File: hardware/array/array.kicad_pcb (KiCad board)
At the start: 2 copper layers, 70 x 100 mm, 165 parts, among them J1 Conn_01x04, J2 Conn_01x05, J3 Conn_01x05, P1 USB_C_Plug_USB2.0, U1 AMS1117-3.3, U2 STM32F103CBTx, Y1 8MHz

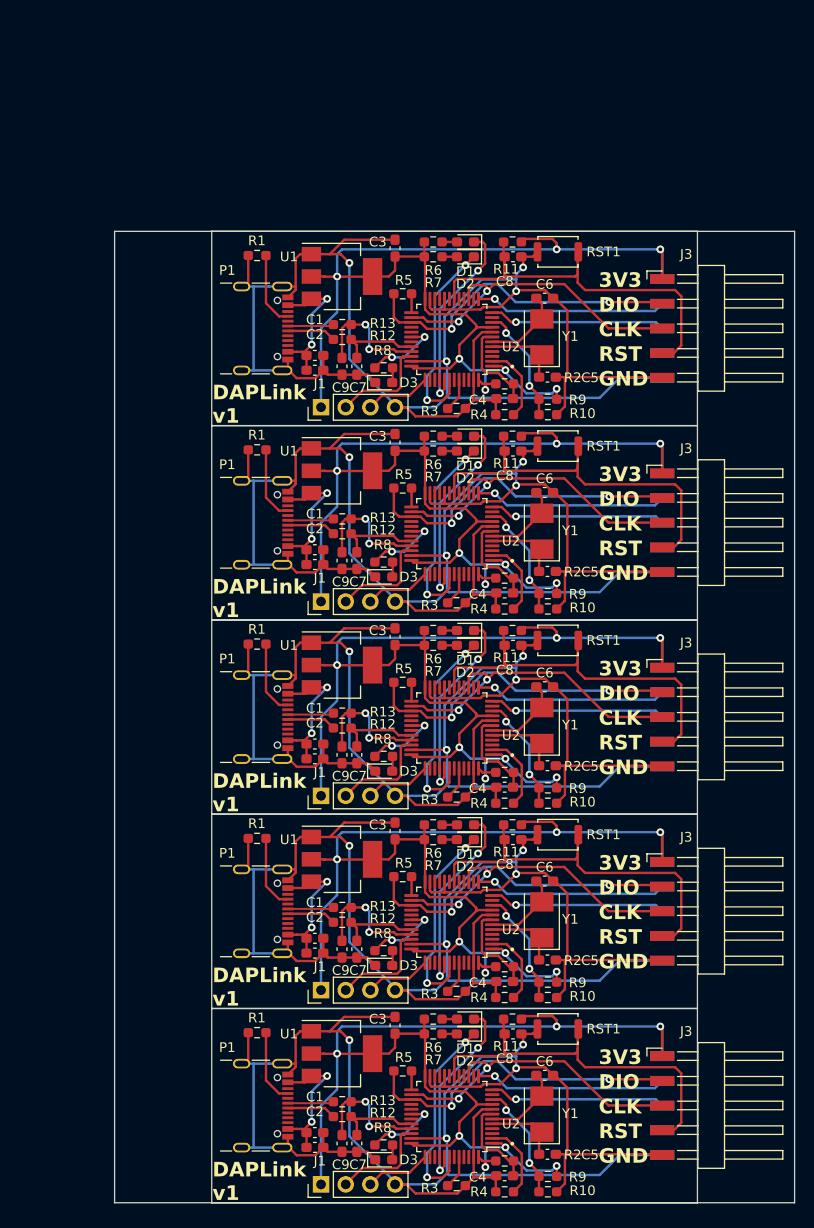
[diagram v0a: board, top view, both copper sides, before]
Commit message: feat(hw/usb): create board array
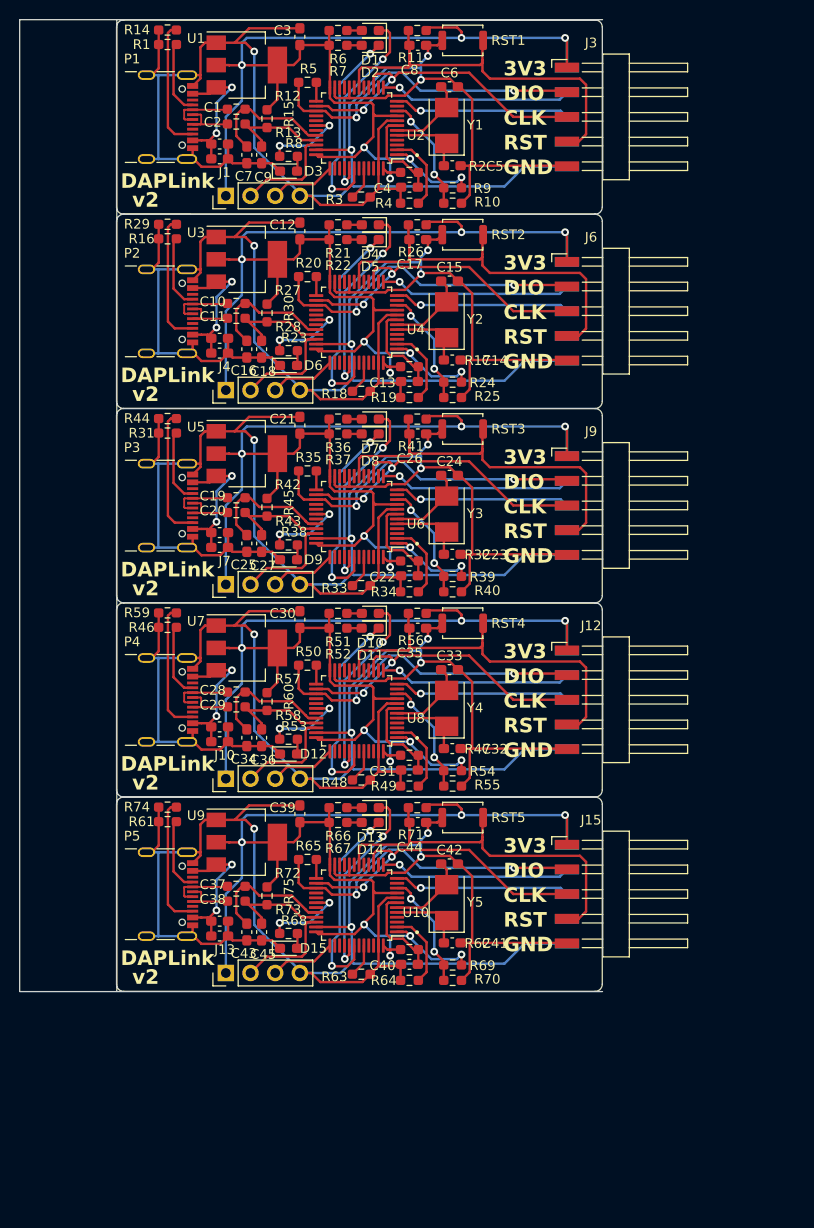
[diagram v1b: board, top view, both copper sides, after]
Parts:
- removed the C1 at (70.6, 82.8)
- removed the C1 at (70.6, 102.8)
- removed the C1 at (70.6, 142.8)
- removed the C1 at (70.6, 162.8)
- removed the C1 at (70.6, 122.8)
- removed the C2 at (70.6, 104.3)
- removed the C2 at (70.6, 144.3)
- removed the C2 at (70.6, 124.3)
- removed the C2 at (70.6, 164.3)
- removed the C2 at (70.6, 84.3)
- removed the C3 at (78.9, 71.7)
- removed the C3 at (78.9, 111.7)
- removed the C3 at (78.9, 131.7)
- removed the C3 at (78.9, 151.7)
- removed the C3 at (78.9, 91.7)
- removed the C4 at (90.2, 167.2)
- removed the C4 at (90.2, 127.2)
- removed the C4 at (90.2, 147.2)
- removed the C4 at (90.2, 107.2)
- removed the C4 at (90.2, 87.2)
- removed the C5 at (94.6, 85.0)
- removed the C5 at (94.6, 105.0)
- removed the C5 at (94.6, 125.0)
- removed the C5 at (94.6, 145.0)
- removed the C5 at (94.6, 165.0)
- removed the C6 at (94.3, 156.9)
- removed the C6 at (94.3, 76.9)
- removed the C6 at (94.3, 136.9)
- removed the C6 at (94.3, 96.9)
- removed the C6 at (94.3, 116.9)
- removed the C7 at (74.9, 83.9)
- removed the C7 at (74.9, 123.9)
- removed the C7 at (74.9, 163.9)
- removed the C7 at (74.9, 143.9)
- removed the C7 at (74.9, 103.9)
- removed the C8 at (91.0, 92.6)
- removed the C8 at (91.0, 132.6)
- removed the C8 at (91.0, 72.6)
- removed the C8 at (91.0, 112.6)
- removed the C8 at (91.0, 152.6)
- removed the C9 at (73.4, 143.9)
- removed the C9 at (73.4, 103.9)
- removed the C9 at (73.4, 123.9)
- removed the C9 at (73.4, 83.9)
- removed the C9 at (73.4, 163.9)
- removed the D1 at (86.1, 151.1)
- removed the D1 at (86.1, 131.1)
- removed the D1 at (86.1, 111.1)
- removed the D1 at (86.1, 71.1)
- removed the D1 at (86.1, 91.1)
- removed the D2 at (86.1, 92.6)
- removed the D2 at (86.1, 112.6)
- removed the D2 at (86.1, 152.6)
- removed the D2 at (86.1, 132.6)
- removed the D2 at (86.1, 72.6)
- removed the D3 at (77.7, 85.6)
- removed the D3 at (77.7, 125.6)
- removed the D3 at (77.7, 165.6)
- removed the D3 at (77.7, 145.6)
- removed the D3 at (77.7, 105.6)
- removed the J1 at (71.3, 88.1)
- removed the J1 at (71.3, 148.1)
- removed the J1 at (71.3, 168.1)
- removed the J1 at (71.3, 108.1)
- removed the J1 at (71.3, 128.1)
- removed the J2 at (111.9, 100.0)
- removed the J2 at (111.9, 140.0)
- removed the J2 at (111.9, 80.0)
- removed the J2 at (111.9, 160.0)
- removed the J2 at (111.9, 120.0)
- removed the J3 at (111.9, 100.0)
- removed the J3 at (111.9, 80.0)
- removed the J3 at (111.9, 140.0)
- removed the J3 at (111.9, 160.0)
- removed the J3 at (111.9, 120.0)
- removed the P1 at (64.2, 120.0)
- removed the P1 at (64.2, 80.0)
- removed the P1 at (64.2, 140.0)
- removed the P1 at (64.2, 160.0)
- removed the P1 at (64.2, 100.0)
- removed the R1 at (64.7, 152.5)
- removed the R1 at (64.7, 112.5)
- removed the R1 at (64.7, 92.5)
- removed the R1 at (64.7, 72.5)
- removed the R1 at (64.7, 132.5)
- removed the R10 at (94.6, 168.9)
- removed the R10 at (94.6, 108.9)
- removed the R10 at (94.6, 88.9)
- removed the R10 at (94.6, 128.9)
- removed the R10 at (94.6, 148.9)
- removed the R11 at (91.0, 151.1)
- removed the R11 at (91.0, 111.1)
- removed the R11 at (91.0, 71.1)
- removed the R11 at (91.0, 91.1)
- removed the R11 at (91.0, 131.1)
- removed the R12 at (73.4, 81.1)
- removed the R12 at (73.4, 121.1)
- removed the R12 at (73.4, 101.1)
- removed the R12 at (73.4, 141.1)
- removed the R12 at (73.4, 161.1)
- removed the R13 at (73.4, 79.6)
- removed the R13 at (73.4, 99.6)
- removed the R13 at (73.4, 159.6)
- removed the R13 at (73.4, 139.6)
- removed the R13 at (73.4, 119.6)
- removed the R2 at (90.2, 105.7)
- removed the R2 at (90.2, 145.7)
- removed the R2 at (90.2, 125.7)
- removed the R2 at (90.2, 85.7)
- removed the R2 at (90.2, 165.7)
- removed the R3 at (85.2, 108.2)
- removed the R3 at (85.2, 88.2)
- removed the R3 at (85.2, 148.2)
- removed the R3 at (85.2, 168.2)
- removed the R3 at (85.2, 128.2)
- removed the R4 at (90.2, 88.9)
- removed the R4 at (90.2, 148.9)
- removed the R4 at (90.2, 108.9)
- removed the R4 at (90.2, 168.9)
- removed the R4 at (90.2, 128.9)
- removed the R5 at (79.7, 136.4)
- removed the R5 at (79.7, 116.4)
- removed the R5 at (79.7, 96.4)
- removed the R5 at (79.7, 156.4)
- removed the R5 at (79.7, 76.4)
- removed the R6 at (82.8, 111.1)
- removed the R6 at (82.8, 151.1)
- removed the R6 at (82.8, 91.1)
- removed the R6 at (82.8, 71.1)
- removed the R6 at (82.8, 131.1)
- removed the R7 at (82.8, 152.6)
- removed the R7 at (82.8, 132.6)
- removed the R7 at (82.8, 92.6)
- removed the R7 at (82.8, 112.6)
- removed the R7 at (82.8, 72.6)
- removed the R8 at (77.7, 104.0)
- removed the R8 at (77.7, 84.0)
- removed the R8 at (77.7, 144.0)
- removed the R8 at (77.7, 164.0)
- removed the R8 at (77.7, 124.0)
- removed the R9 at (94.6, 87.3)
- removed the R9 at (94.6, 127.3)
- removed the R9 at (94.6, 107.3)
- removed the R9 at (94.6, 167.3)
- removed the R9 at (94.6, 147.3)
- removed the RST1 at (95.6, 72.1)
- removed the RST1 at (95.6, 92.1)
- removed the RST1 at (95.6, 132.1)
- removed the RST1 at (95.6, 152.1)
- removed the RST1 at (95.6, 112.1)
- removed the U1 at (73.4, 114.6)
- removed the U1 at (73.4, 94.6)
- removed the U1 at (73.4, 154.6)
- removed the U1 at (73.4, 74.6)
- removed the U1 at (73.4, 134.6)
- removed the U2 at (84.7, 161.1)
- removed the U2 at (84.7, 141.1)
- removed the U2 at (84.7, 101.1)
- removed the U2 at (84.7, 81.1)
- removed the U2 at (84.7, 121.1)
- removed the Y1 at (94.0, 100.9)
- removed the Y1 at (94.0, 80.9)
- removed the Y1 at (94.0, 160.9)
- removed the Y1 at (94.0, 140.9)
- removed the Y1 at (94.0, 120.9)
- added C1: 10nF, Capacitor_SMD:C_0603_1608Metric_Pad1.08x0.95mm_HandSolder, F.Cu at (60.8, 61.0)
- added C10: 10nF, Capacitor_SMD:C_0603_1608Metric_Pad1.08x0.95mm_HandSolder, F.Cu at (60.8, 81.0)
- added C11: 10uF, Capacitor_SMD:C_0603_1608Metric_Pad1.08x0.95mm_HandSolder, F.Cu at (60.8, 82.5)
- added C12: 10uF, Capacitor_SMD:C_0603_1608Metric_Pad1.08x0.95mm_HandSolder, F.Cu at (69.1, 70.0)
- added C13: 10nF, Capacitor_SMD:C_0603_1608Metric_Pad1.08x0.95mm_HandSolder, F.Cu at (80.4, 85.5)
- added C14: 20pF, Capacitor_SMD:C_0603_1608Metric_Pad1.08x0.95mm_HandSolder, F.Cu at (84.8, 83.2)
- added C15: 20pF, Capacitor_SMD:C_0603_1608Metric_Pad1.08x0.95mm_HandSolder, F.Cu at (84.5, 75.1)
- added C16: 18pF, Capacitor_SMD:C_0603_1608Metric_Pad1.08x0.95mm_HandSolder, F.Cu at (63.6, 82.1)
- added C17: 10nF, Capacitor_SMD:C_0603_1608Metric_Pad1.08x0.95mm_HandSolder, F.Cu at (81.2, 70.9)
- added C18: 18pF, Capacitor_SMD:C_0603_1608Metric_Pad1.08x0.95mm_HandSolder, F.Cu at (65.1, 82.1)
- added C19: 10nF, Capacitor_SMD:C_0603_1608Metric_Pad1.08x0.95mm_HandSolder, F.Cu at (60.8, 101.0)
- added C2: 10uF, Capacitor_SMD:C_0603_1608Metric_Pad1.08x0.95mm_HandSolder, F.Cu at (60.8, 62.5)
- added C20: 10uF, Capacitor_SMD:C_0603_1608Metric_Pad1.08x0.95mm_HandSolder, F.Cu at (60.8, 102.5)
- added C21: 10uF, Capacitor_SMD:C_0603_1608Metric_Pad1.08x0.95mm_HandSolder, F.Cu at (69.1, 90.0)
- added C22: 10nF, Capacitor_SMD:C_0603_1608Metric_Pad1.08x0.95mm_HandSolder, F.Cu at (80.4, 105.5)
- added C23: 20pF, Capacitor_SMD:C_0603_1608Metric_Pad1.08x0.95mm_HandSolder, F.Cu at (84.8, 103.2)
- added C24: 20pF, Capacitor_SMD:C_0603_1608Metric_Pad1.08x0.95mm_HandSolder, F.Cu at (84.5, 95.1)
- added C25: 18pF, Capacitor_SMD:C_0603_1608Metric_Pad1.08x0.95mm_HandSolder, F.Cu at (63.6, 102.1)
- added C26: 10nF, Capacitor_SMD:C_0603_1608Metric_Pad1.08x0.95mm_HandSolder, F.Cu at (81.2, 90.9)
- added C27: 18pF, Capacitor_SMD:C_0603_1608Metric_Pad1.08x0.95mm_HandSolder, F.Cu at (65.1, 102.1)
- added C28: 10nF, Capacitor_SMD:C_0603_1608Metric_Pad1.08x0.95mm_HandSolder, F.Cu at (60.8, 121.0)
- added C29: 10uF, Capacitor_SMD:C_0603_1608Metric_Pad1.08x0.95mm_HandSolder, F.Cu at (60.8, 122.5)
- added C3: 10uF, Capacitor_SMD:C_0603_1608Metric_Pad1.08x0.95mm_HandSolder, F.Cu at (69.1, 50.0)
- added C30: 10uF, Capacitor_SMD:C_0603_1608Metric_Pad1.08x0.95mm_HandSolder, F.Cu at (69.1, 110.0)
- added C31: 10nF, Capacitor_SMD:C_0603_1608Metric_Pad1.08x0.95mm_HandSolder, F.Cu at (80.4, 125.5)
- added C32: 20pF, Capacitor_SMD:C_0603_1608Metric_Pad1.08x0.95mm_HandSolder, F.Cu at (84.8, 123.2)
- added C33: 20pF, Capacitor_SMD:C_0603_1608Metric_Pad1.08x0.95mm_HandSolder, F.Cu at (84.5, 115.1)
- added C34: 18pF, Capacitor_SMD:C_0603_1608Metric_Pad1.08x0.95mm_HandSolder, F.Cu at (63.6, 122.1)
- added C35: 10nF, Capacitor_SMD:C_0603_1608Metric_Pad1.08x0.95mm_HandSolder, F.Cu at (81.2, 110.9)
- added C36: 18pF, Capacitor_SMD:C_0603_1608Metric_Pad1.08x0.95mm_HandSolder, F.Cu at (65.1, 122.1)
- added C37: 10nF, Capacitor_SMD:C_0603_1608Metric_Pad1.08x0.95mm_HandSolder, F.Cu at (60.8, 141.0)
- added C38: 10uF, Capacitor_SMD:C_0603_1608Metric_Pad1.08x0.95mm_HandSolder, F.Cu at (60.8, 142.5)
- added C39: 10uF, Capacitor_SMD:C_0603_1608Metric_Pad1.08x0.95mm_HandSolder, F.Cu at (69.1, 130.0)
- added C4: 10nF, Capacitor_SMD:C_0603_1608Metric_Pad1.08x0.95mm_HandSolder, F.Cu at (80.4, 65.5)
- added C40: 10nF, Capacitor_SMD:C_0603_1608Metric_Pad1.08x0.95mm_HandSolder, F.Cu at (80.4, 145.5)
- added C41: 20pF, Capacitor_SMD:C_0603_1608Metric_Pad1.08x0.95mm_HandSolder, F.Cu at (84.8, 143.2)
- added C42: 20pF, Capacitor_SMD:C_0603_1608Metric_Pad1.08x0.95mm_HandSolder, F.Cu at (84.5, 135.1)
- added C43: 18pF, Capacitor_SMD:C_0603_1608Metric_Pad1.08x0.95mm_HandSolder, F.Cu at (63.6, 142.1)
- added C44: 10nF, Capacitor_SMD:C_0603_1608Metric_Pad1.08x0.95mm_HandSolder, F.Cu at (81.2, 130.9)
- added C45: 18pF, Capacitor_SMD:C_0603_1608Metric_Pad1.08x0.95mm_HandSolder, F.Cu at (65.1, 142.1)
- added C5: 20pF, Capacitor_SMD:C_0603_1608Metric_Pad1.08x0.95mm_HandSolder, F.Cu at (84.8, 63.2)
- added C6: 20pF, Capacitor_SMD:C_0603_1608Metric_Pad1.08x0.95mm_HandSolder, F.Cu at (84.5, 55.1)
- added C7: 18pF, Capacitor_SMD:C_0603_1608Metric_Pad1.08x0.95mm_HandSolder, F.Cu at (63.6, 62.1)
- added C8: 10nF, Capacitor_SMD:C_0603_1608Metric_Pad1.08x0.95mm_HandSolder, F.Cu at (81.2, 50.9)
- added C9: 18pF, Capacitor_SMD:C_0603_1608Metric_Pad1.08x0.95mm_HandSolder, F.Cu at (65.1, 62.1)
- added D1: LEDG, LED_SMD:LED_0603_1608Metric_Pad1.05x0.95mm_HandSolder, F.Cu at (76.3, 49.3)
- added D10: LEDG, LED_SMD:LED_0603_1608Metric_Pad1.05x0.95mm_HandSolder, F.Cu at (76.3, 109.3)
- added D11: LEDB, LED_SMD:LED_0603_1608Metric_Pad1.05x0.95mm_HandSolder, F.Cu at (76.3, 110.9)
- added D12: LEDR, LED_SMD:LED_0603_1608Metric_Pad1.05x0.95mm_HandSolder, F.Cu at (67.9, 123.8)
- added D13: LEDG, LED_SMD:LED_0603_1608Metric_Pad1.05x0.95mm_HandSolder, F.Cu at (76.3, 129.3)
- added D14: LEDB, LED_SMD:LED_0603_1608Metric_Pad1.05x0.95mm_HandSolder, F.Cu at (76.3, 130.9)
- added D15: LEDR, LED_SMD:LED_0603_1608Metric_Pad1.05x0.95mm_HandSolder, F.Cu at (67.9, 143.8)
- added D2: LEDB, LED_SMD:LED_0603_1608Metric_Pad1.05x0.95mm_HandSolder, F.Cu at (76.3, 50.9)
- added D3: LEDR, LED_SMD:LED_0603_1608Metric_Pad1.05x0.95mm_HandSolder, F.Cu at (67.9, 63.8)
- added D4: LEDG, LED_SMD:LED_0603_1608Metric_Pad1.05x0.95mm_HandSolder, F.Cu at (76.3, 69.3)
- added D5: LEDB, LED_SMD:LED_0603_1608Metric_Pad1.05x0.95mm_HandSolder, F.Cu at (76.3, 70.9)
- added D6: LEDR, LED_SMD:LED_0603_1608Metric_Pad1.05x0.95mm_HandSolder, F.Cu at (67.9, 83.8)
- added D7: LEDG, LED_SMD:LED_0603_1608Metric_Pad1.05x0.95mm_HandSolder, F.Cu at (76.3, 89.3)
- added D8: LEDB, LED_SMD:LED_0603_1608Metric_Pad1.05x0.95mm_HandSolder, F.Cu at (76.3, 90.9)
- added D9: LEDR, LED_SMD:LED_0603_1608Metric_Pad1.05x0.95mm_HandSolder, F.Cu at (67.9, 103.8)
- added J1: Conn_01x04, Connector_PinHeader_2.54mm:PinHeader_1x04_P2.54mm_Vertical, F.Cu at (61.5, 66.3)
- added J10: Conn_01x04, Connector_PinHeader_2.54mm:PinHeader_1x04_P2.54mm_Vertical, F.Cu at (61.5, 126.3)
- added J11: Conn_01x05, Connector_Harwin:Harwin_M20-89005xx_1x05_P2.54mm_Horizontal, B.Cu at (102.1, 118.2)
- added J12: Conn_01x05, Connector_Harwin:Harwin_M20-89005xx_1x05_P2.54mm_Horizontal, F.Cu at (102.1, 118.2)
- added J13: Conn_01x04, Connector_PinHeader_2.54mm:PinHeader_1x04_P2.54mm_Vertical, F.Cu at (61.5, 146.3)
- added J14: Conn_01x05, Connector_Harwin:Harwin_M20-89005xx_1x05_P2.54mm_Horizontal, B.Cu at (102.1, 138.2)
- added J15: Conn_01x05, Connector_Harwin:Harwin_M20-89005xx_1x05_P2.54mm_Horizontal, F.Cu at (102.1, 138.2)
- added J2: Conn_01x05, Connector_Harwin:Harwin_M20-89005xx_1x05_P2.54mm_Horizontal, B.Cu at (102.1, 58.2)
- added J3: Conn_01x05, Connector_Harwin:Harwin_M20-89005xx_1x05_P2.54mm_Horizontal, F.Cu at (102.1, 58.2)
- added J4: Conn_01x04, Connector_PinHeader_2.54mm:PinHeader_1x04_P2.54mm_Vertical, F.Cu at (61.5, 86.3)
- added J5: Conn_01x05, Connector_Harwin:Harwin_M20-89005xx_1x05_P2.54mm_Horizontal, B.Cu at (102.1, 78.2)
- added J6: Conn_01x05, Connector_Harwin:Harwin_M20-89005xx_1x05_P2.54mm_Horizontal, F.Cu at (102.1, 78.2)
- added J7: Conn_01x04, Connector_PinHeader_2.54mm:PinHeader_1x04_P2.54mm_Vertical, F.Cu at (61.5, 106.3)
- added J8: Conn_01x05, Connector_Harwin:Harwin_M20-89005xx_1x05_P2.54mm_Horizontal, B.Cu at (102.1, 98.2)
- added J9: Conn_01x05, Connector_Harwin:Harwin_M20-89005xx_1x05_P2.54mm_Horizontal, F.Cu at (102.1, 98.2)
- added P1: USB_C_Receptacle_USB2.0, Connector_USB:USB_C_Receptacle_GCT_USB4105-xx-A_16P_TopMnt_Horizontal, F.Cu at (54.4, 58.2)
- added P2: USB_C_Receptacle_USB2.0, Connector_USB:USB_C_Receptacle_GCT_USB4105-xx-A_16P_TopMnt_Horizontal, F.Cu at (54.4, 78.2)
- added P3: USB_C_Receptacle_USB2.0, Connector_USB:USB_C_Receptacle_GCT_USB4105-xx-A_16P_TopMnt_Horizontal, F.Cu at (54.4, 98.2)
- added P4: USB_C_Receptacle_USB2.0, Connector_USB:USB_C_Receptacle_GCT_USB4105-xx-A_16P_TopMnt_Horizontal, F.Cu at (54.4, 118.2)
- added P5: USB_C_Receptacle_USB2.0, Connector_USB:USB_C_Receptacle_GCT_USB4105-xx-A_16P_TopMnt_Horizontal, F.Cu at (54.4, 138.2)
- added R1: 5K1, Resistor_SMD:R_0603_1608Metric_Pad0.98x0.95mm_HandSolder, F.Cu at (55.5, 50.8)
- added R10: 4K7, Resistor_SMD:R_0603_1608Metric_Pad0.98x0.95mm_HandSolder, F.Cu at (84.8, 67.1)
- added R11: 10K, Resistor_SMD:R_0603_1608Metric_Pad0.98x0.95mm_HandSolder, F.Cu at (81.2, 49.3)
- added R12: 33, Resistor_SMD:R_0603_1608Metric_Pad0.98x0.95mm_HandSolder, F.Cu at (62.5, 57.4)
- added R13: 33, Resistor_SMD:R_0603_1608Metric_Pad0.98x0.95mm_HandSolder, F.Cu at (62.5, 59.0)
- added R14: 5K1, Resistor_SMD:R_0603_1608Metric_Pad0.98x0.95mm_HandSolder, F.Cu at (55.5, 49.3)
- added R15: 1K5, Resistor_SMD:R_0603_1608Metric_Pad0.98x0.95mm_HandSolder, F.Cu at (65.7, 58.4)
- added R16: 5K1, Resistor_SMD:R_0603_1608Metric_Pad0.98x0.95mm_HandSolder, F.Cu at (55.5, 70.8)
- added R17: 10K, Resistor_SMD:R_0603_1608Metric_Pad0.98x0.95mm_HandSolder, F.Cu at (80.4, 83.9)
- added R18: 10K, Resistor_SMD:R_0603_1608Metric_Pad0.98x0.95mm_HandSolder, F.Cu at (75.4, 86.5)
- added R19: 10K, Resistor_SMD:R_0603_1608Metric_Pad0.98x0.95mm_HandSolder, F.Cu at (80.4, 87.1)
- added R2: 10K, Resistor_SMD:R_0603_1608Metric_Pad0.98x0.95mm_HandSolder, F.Cu at (80.4, 63.9)
- added R20: 100, Resistor_SMD:R_0603_1608Metric_Pad0.98x0.95mm_HandSolder, F.Cu at (69.9, 74.7)
- added R21: 1K5, Resistor_SMD:R_0603_1608Metric_Pad0.98x0.95mm_HandSolder, F.Cu at (73.0, 69.3)
- added R22: 1K5, Resistor_SMD:R_0603_1608Metric_Pad0.98x0.95mm_HandSolder, F.Cu at (73.0, 70.9)
- added R23: 470, Resistor_SMD:R_0603_1608Metric_Pad0.98x0.95mm_HandSolder, F.Cu at (67.9, 82.3)
- added R24: 4K7, Resistor_SMD:R_0603_1608Metric_Pad0.98x0.95mm_HandSolder, F.Cu at (84.8, 85.5)
- added R25: 4K7, Resistor_SMD:R_0603_1608Metric_Pad0.98x0.95mm_HandSolder, F.Cu at (84.8, 87.1)
- added R26: 10K, Resistor_SMD:R_0603_1608Metric_Pad0.98x0.95mm_HandSolder, F.Cu at (81.2, 69.3)
- added R27: 33, Resistor_SMD:R_0603_1608Metric_Pad0.98x0.95mm_HandSolder, F.Cu at (62.5, 77.4)
- added R28: 33, Resistor_SMD:R_0603_1608Metric_Pad0.98x0.95mm_HandSolder, F.Cu at (62.5, 79.0)
- added R29: 5K1, Resistor_SMD:R_0603_1608Metric_Pad0.98x0.95mm_HandSolder, F.Cu at (55.5, 69.3)
- added R3: 10K, Resistor_SMD:R_0603_1608Metric_Pad0.98x0.95mm_HandSolder, F.Cu at (75.4, 66.5)
- added R30: 1K5, Resistor_SMD:R_0603_1608Metric_Pad0.98x0.95mm_HandSolder, F.Cu at (65.7, 78.4)
- added R31: 5K1, Resistor_SMD:R_0603_1608Metric_Pad0.98x0.95mm_HandSolder, F.Cu at (55.5, 90.8)
- added R32: 10K, Resistor_SMD:R_0603_1608Metric_Pad0.98x0.95mm_HandSolder, F.Cu at (80.4, 103.9)
- added R33: 10K, Resistor_SMD:R_0603_1608Metric_Pad0.98x0.95mm_HandSolder, F.Cu at (75.4, 106.5)
- added R34: 10K, Resistor_SMD:R_0603_1608Metric_Pad0.98x0.95mm_HandSolder, F.Cu at (80.4, 107.1)
- added R35: 100, Resistor_SMD:R_0603_1608Metric_Pad0.98x0.95mm_HandSolder, F.Cu at (69.9, 94.7)
- added R36: 1K5, Resistor_SMD:R_0603_1608Metric_Pad0.98x0.95mm_HandSolder, F.Cu at (73.0, 89.3)
- added R37: 1K5, Resistor_SMD:R_0603_1608Metric_Pad0.98x0.95mm_HandSolder, F.Cu at (73.0, 90.9)
- added R38: 470, Resistor_SMD:R_0603_1608Metric_Pad0.98x0.95mm_HandSolder, F.Cu at (67.9, 102.3)
- added R39: 4K7, Resistor_SMD:R_0603_1608Metric_Pad0.98x0.95mm_HandSolder, F.Cu at (84.8, 105.5)
- added R4: 10K, Resistor_SMD:R_0603_1608Metric_Pad0.98x0.95mm_HandSolder, F.Cu at (80.4, 67.1)
- added R40: 4K7, Resistor_SMD:R_0603_1608Metric_Pad0.98x0.95mm_HandSolder, F.Cu at (84.8, 107.1)
- added R41: 10K, Resistor_SMD:R_0603_1608Metric_Pad0.98x0.95mm_HandSolder, F.Cu at (81.2, 89.3)
- added R42: 33, Resistor_SMD:R_0603_1608Metric_Pad0.98x0.95mm_HandSolder, F.Cu at (62.5, 97.4)
- added R43: 33, Resistor_SMD:R_0603_1608Metric_Pad0.98x0.95mm_HandSolder, F.Cu at (62.5, 99.0)
- added R44: 5K1, Resistor_SMD:R_0603_1608Metric_Pad0.98x0.95mm_HandSolder, F.Cu at (55.5, 89.3)
- added R45: 1K5, Resistor_SMD:R_0603_1608Metric_Pad0.98x0.95mm_HandSolder, F.Cu at (65.7, 98.4)
- added R46: 5K1, Resistor_SMD:R_0603_1608Metric_Pad0.98x0.95mm_HandSolder, F.Cu at (55.5, 110.8)
- added R47: 10K, Resistor_SMD:R_0603_1608Metric_Pad0.98x0.95mm_HandSolder, F.Cu at (80.4, 123.9)
- added R48: 10K, Resistor_SMD:R_0603_1608Metric_Pad0.98x0.95mm_HandSolder, F.Cu at (75.4, 126.5)
- added R49: 10K, Resistor_SMD:R_0603_1608Metric_Pad0.98x0.95mm_HandSolder, F.Cu at (80.4, 127.1)
- added R5: 100, Resistor_SMD:R_0603_1608Metric_Pad0.98x0.95mm_HandSolder, F.Cu at (69.9, 54.7)
- added R50: 100, Resistor_SMD:R_0603_1608Metric_Pad0.98x0.95mm_HandSolder, F.Cu at (69.9, 114.7)
- added R51: 1K5, Resistor_SMD:R_0603_1608Metric_Pad0.98x0.95mm_HandSolder, F.Cu at (73.0, 109.3)
- added R52: 1K5, Resistor_SMD:R_0603_1608Metric_Pad0.98x0.95mm_HandSolder, F.Cu at (73.0, 110.9)
- added R53: 470, Resistor_SMD:R_0603_1608Metric_Pad0.98x0.95mm_HandSolder, F.Cu at (67.9, 122.3)
- added R54: 4K7, Resistor_SMD:R_0603_1608Metric_Pad0.98x0.95mm_HandSolder, F.Cu at (84.8, 125.5)
- added R55: 4K7, Resistor_SMD:R_0603_1608Metric_Pad0.98x0.95mm_HandSolder, F.Cu at (84.8, 127.1)
- added R56: 10K, Resistor_SMD:R_0603_1608Metric_Pad0.98x0.95mm_HandSolder, F.Cu at (81.2, 109.3)
- added R57: 33, Resistor_SMD:R_0603_1608Metric_Pad0.98x0.95mm_HandSolder, F.Cu at (62.5, 117.4)
- added R58: 33, Resistor_SMD:R_0603_1608Metric_Pad0.98x0.95mm_HandSolder, F.Cu at (62.5, 119.0)
- added R59: 5K1, Resistor_SMD:R_0603_1608Metric_Pad0.98x0.95mm_HandSolder, F.Cu at (55.5, 109.3)
- added R6: 1K5, Resistor_SMD:R_0603_1608Metric_Pad0.98x0.95mm_HandSolder, F.Cu at (73.0, 49.3)
- added R60: 1K5, Resistor_SMD:R_0603_1608Metric_Pad0.98x0.95mm_HandSolder, F.Cu at (65.7, 118.4)
- added R61: 5K1, Resistor_SMD:R_0603_1608Metric_Pad0.98x0.95mm_HandSolder, F.Cu at (55.5, 130.8)
- added R62: 10K, Resistor_SMD:R_0603_1608Metric_Pad0.98x0.95mm_HandSolder, F.Cu at (80.4, 143.9)
- added R63: 10K, Resistor_SMD:R_0603_1608Metric_Pad0.98x0.95mm_HandSolder, F.Cu at (75.4, 146.5)
- added R64: 10K, Resistor_SMD:R_0603_1608Metric_Pad0.98x0.95mm_HandSolder, F.Cu at (80.4, 147.1)
- added R65: 100, Resistor_SMD:R_0603_1608Metric_Pad0.98x0.95mm_HandSolder, F.Cu at (69.9, 134.7)
- added R66: 1K5, Resistor_SMD:R_0603_1608Metric_Pad0.98x0.95mm_HandSolder, F.Cu at (73.0, 129.3)
- added R67: 1K5, Resistor_SMD:R_0603_1608Metric_Pad0.98x0.95mm_HandSolder, F.Cu at (73.0, 130.9)
- added R68: 470, Resistor_SMD:R_0603_1608Metric_Pad0.98x0.95mm_HandSolder, F.Cu at (67.9, 142.3)
- added R69: 4K7, Resistor_SMD:R_0603_1608Metric_Pad0.98x0.95mm_HandSolder, F.Cu at (84.8, 145.5)
- added R7: 1K5, Resistor_SMD:R_0603_1608Metric_Pad0.98x0.95mm_HandSolder, F.Cu at (73.0, 50.9)
- added R70: 4K7, Resistor_SMD:R_0603_1608Metric_Pad0.98x0.95mm_HandSolder, F.Cu at (84.8, 147.1)
- added R71: 10K, Resistor_SMD:R_0603_1608Metric_Pad0.98x0.95mm_HandSolder, F.Cu at (81.2, 129.3)
- added R72: 33, Resistor_SMD:R_0603_1608Metric_Pad0.98x0.95mm_HandSolder, F.Cu at (62.5, 137.4)
- added R73: 33, Resistor_SMD:R_0603_1608Metric_Pad0.98x0.95mm_HandSolder, F.Cu at (62.5, 138.9)
- added R74: 5K1, Resistor_SMD:R_0603_1608Metric_Pad0.98x0.95mm_HandSolder, F.Cu at (55.5, 129.3)
- added R75: 1K5, Resistor_SMD:R_0603_1608Metric_Pad0.98x0.95mm_HandSolder, F.Cu at (65.7, 138.4)
- added R8: 470, Resistor_SMD:R_0603_1608Metric_Pad0.98x0.95mm_HandSolder, F.Cu at (67.9, 62.3)
- added R9: 4K7, Resistor_SMD:R_0603_1608Metric_Pad0.98x0.95mm_HandSolder, F.Cu at (84.8, 65.5)
- added RST1: RST, Button_Switch_SMD:SW_Push_SPST_NO_Alps_SKRK, F.Cu at (85.8, 50.3)
- added RST2: RST, Button_Switch_SMD:SW_Push_SPST_NO_Alps_SKRK, F.Cu at (85.8, 70.3)
- added RST3: RST, Button_Switch_SMD:SW_Push_SPST_NO_Alps_SKRK, F.Cu at (85.8, 90.3)
- added RST4: RST, Button_Switch_SMD:SW_Push_SPST_NO_Alps_SKRK, F.Cu at (85.8, 110.3)
- added RST5: RST, Button_Switch_SMD:SW_Push_SPST_NO_Alps_SKRK, F.Cu at (85.8, 130.3)
- added U1: AMS1117-3.3, Package_TO_SOT_SMD:SOT-223-3_TabPin2, F.Cu at (63.6, 52.9)
- added U10: STM32F103CBTx, Package_QFP:LQFP-48_7x7mm_P0.5mm, F.Cu at (74.9, 139.4)
- added U2: STM32F103CBTx, Package_QFP:LQFP-48_7x7mm_P0.5mm, F.Cu at (74.9, 59.4)
- added U3: AMS1117-3.3, Package_TO_SOT_SMD:SOT-223-3_TabPin2, F.Cu at (63.6, 72.9)
- added U4: STM32F103CBTx, Package_QFP:LQFP-48_7x7mm_P0.5mm, F.Cu at (74.9, 79.4)
- added U5: AMS1117-3.3, Package_TO_SOT_SMD:SOT-223-3_TabPin2, F.Cu at (63.6, 92.9)
- added U6: STM32F103CBTx, Package_QFP:LQFP-48_7x7mm_P0.5mm, F.Cu at (74.9, 99.4)
- added U7: AMS1117-3.3, Package_TO_SOT_SMD:SOT-223-3_TabPin2, F.Cu at (63.6, 112.9)
- added U8: STM32F103CBTx, Package_QFP:LQFP-48_7x7mm_P0.5mm, F.Cu at (74.9, 119.4)
- added U9: AMS1117-3.3, Package_TO_SOT_SMD:SOT-223-3_TabPin2, F.Cu at (63.6, 132.9)
- added Y1: 8MHz, Crystal:Crystal_SMD_5032-2Pin_5.0x3.2mm, F.Cu at (84.2, 59.1)
- added Y2: 8MHz, Crystal:Crystal_SMD_5032-2Pin_5.0x3.2mm, F.Cu at (84.2, 79.1)
- added Y3: 8MHz, Crystal:Crystal_SMD_5032-2Pin_5.0x3.2mm, F.Cu at (84.2, 99.1)
- added Y4: 8MHz, Crystal:Crystal_SMD_5032-2Pin_5.0x3.2mm, F.Cu at (84.2, 119.1)
- added Y5: 8MHz, Crystal:Crystal_SMD_5032-2Pin_5.0x3.2mm, F.Cu at (84.2, 139.1)
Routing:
- net Net-(P1-CC2): track 0.00 -> 67.7 mm
- net Net-(P1-CC): track 38.6 -> 0.00 mm
- net Net-(P1-CC1): track 0.00 -> 38.3 mm
- net +3.3V: track 589.5 -> 616.0 mm
- net /PA11: track 43.3 -> 66.4 mm
- net /PA12: track 63.8 -> 55.1 mm, vias 10 -> 0
- net GND: track 935.9 -> 944.3 mm
- net /D+: track 23.7 -> 31.4 mm
- net /D-: track 25.2 -> 31.4 mm
- net /PA9: track 39.0 -> 42.2 mm
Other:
- board size 70 x 100 mm -> 60 x 100 mm
- board text added: "DAPLink"
- board text added: "v2"
- board text removed: "DAPLink v1"
